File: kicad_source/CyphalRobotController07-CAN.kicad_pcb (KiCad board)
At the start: 2 copper layers, 140 x 70 mm, 163 parts, among them J1 BM04B-SRSS-TB, J10 x, J11 PowerPole, J12 Conn_01x02, J13 Conn_01x02, J14 Conn_01x02, J15 PinHeader_1x04, J16 PinHeader_1x04, J17 PinHeader_1x05, J18 Conn_01x02, J2 RASPBERRYPI_PICO, J3 BM04B-SRSS-TB, J4 B3B-PH-SM4-TB, J5 BM04B-GHS-TBT, J6 BM04B-GHS-TBT, J7 x, J8 x, J9 x, Q1 2N7002, Q2 IPD90P03P4L- 04, SW1 PTS636 SM43 SMTR LFS, U1 24LC64-I/SN, U10 ADS1015IDGS, U11 OPA2374AIDCN, U12 INA226, U13 IFX91041EFJ, U14 ITS4200S-ME-P, U15 ITS4200S-ME-P, U16 BNO085, U2 MCP2515-I/SO, U3 SN65HVD232, U4 74xx08, U5 IFX007T, U6 IFX007T, U7 IFX007T, U8 IFX007T, U9 OPA2374AIDCN, Y1 RH100-16.000-16-3030-EXT-TR, Y2 DNI

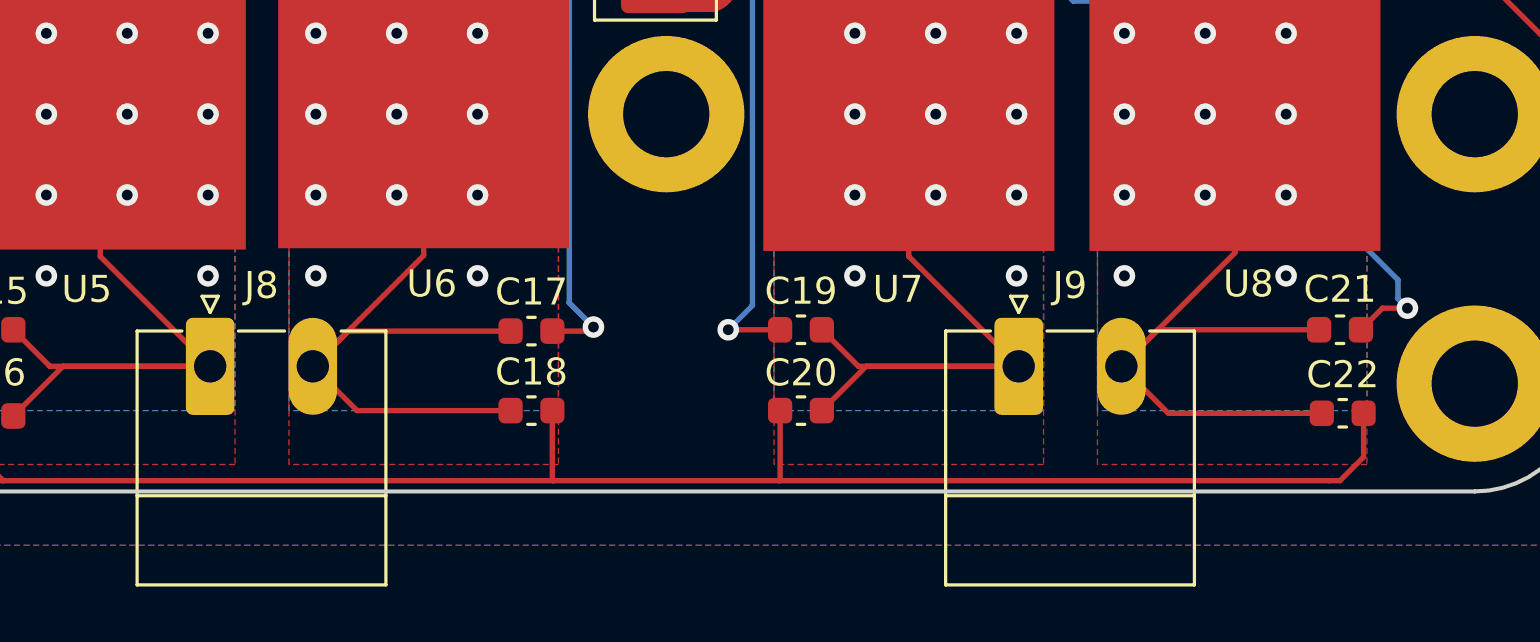
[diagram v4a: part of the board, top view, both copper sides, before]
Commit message: added JST XH connector for motor and encoder
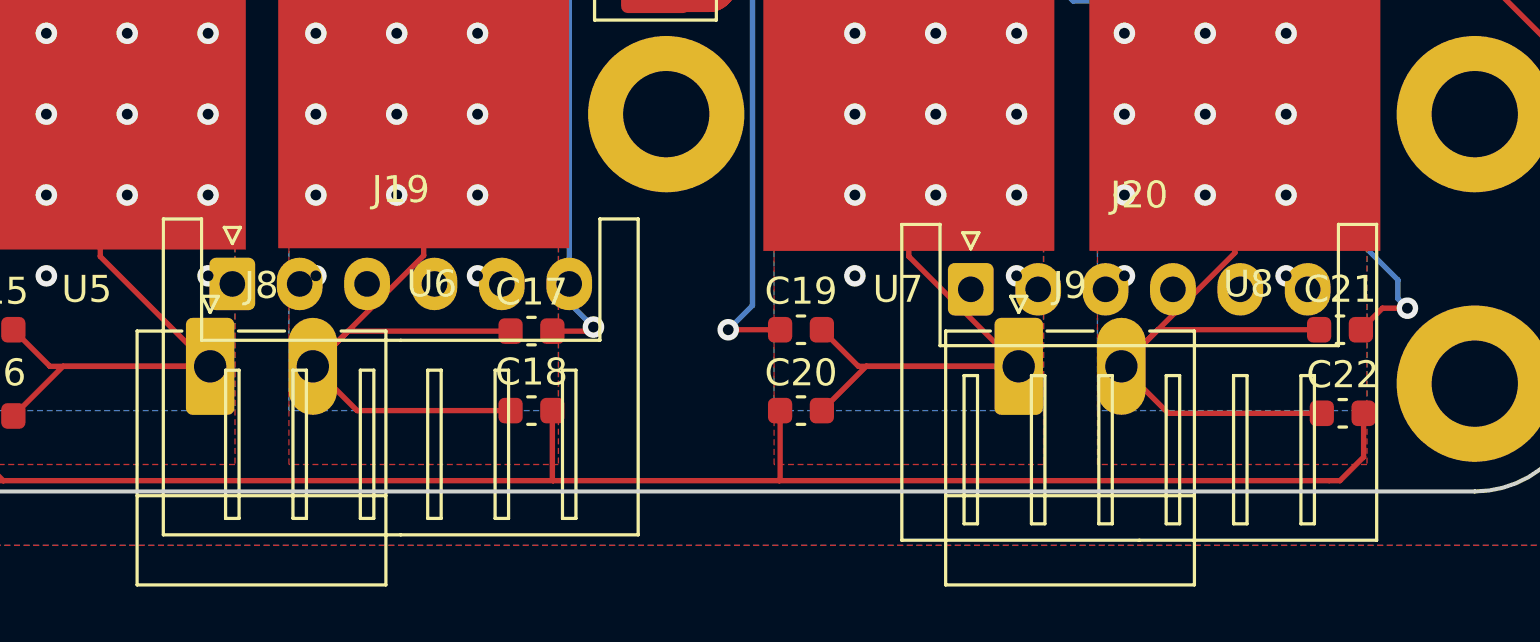
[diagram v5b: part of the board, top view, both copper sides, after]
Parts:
- added J19: S6B-XH-A, Connector_JST:JST_XH_S6B-XH-A_1x06_P2.50mm_Horizontal, F.Cu at (140.9, 118.3)
- added J20: S6B-XH-A, Connector_JST:JST_XH_S6B-XH-A_1x06_P2.50mm_Horizontal, F.Cu at (168.3, 118.5)
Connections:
- net /QUAD0 renamed QUAD0
- net /QUAD1 renamed QUAD1
- net /QUAD2 renamed QUAD2
- net /QUAD3 renamed QUAD3
